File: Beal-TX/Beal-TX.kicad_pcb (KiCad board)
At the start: 2 copper layers, 37.1 x 56.9 mm, 64 parts, among them J1 CONMHF1-SMD-T, J3 Conn_02x04_Odd_Even, J4 Conn_02x04_Odd_Even, J5 UJ20-C-H-G-MSMT-4B-P16-TR, J6 Screw_Terminal_01x06, J7 TC2050, SW2 SW_Push, U150 LM5157-Q1, U2 TPSM863253, U5 LoRa-E5, U6 DRV8912QPWPRQ1

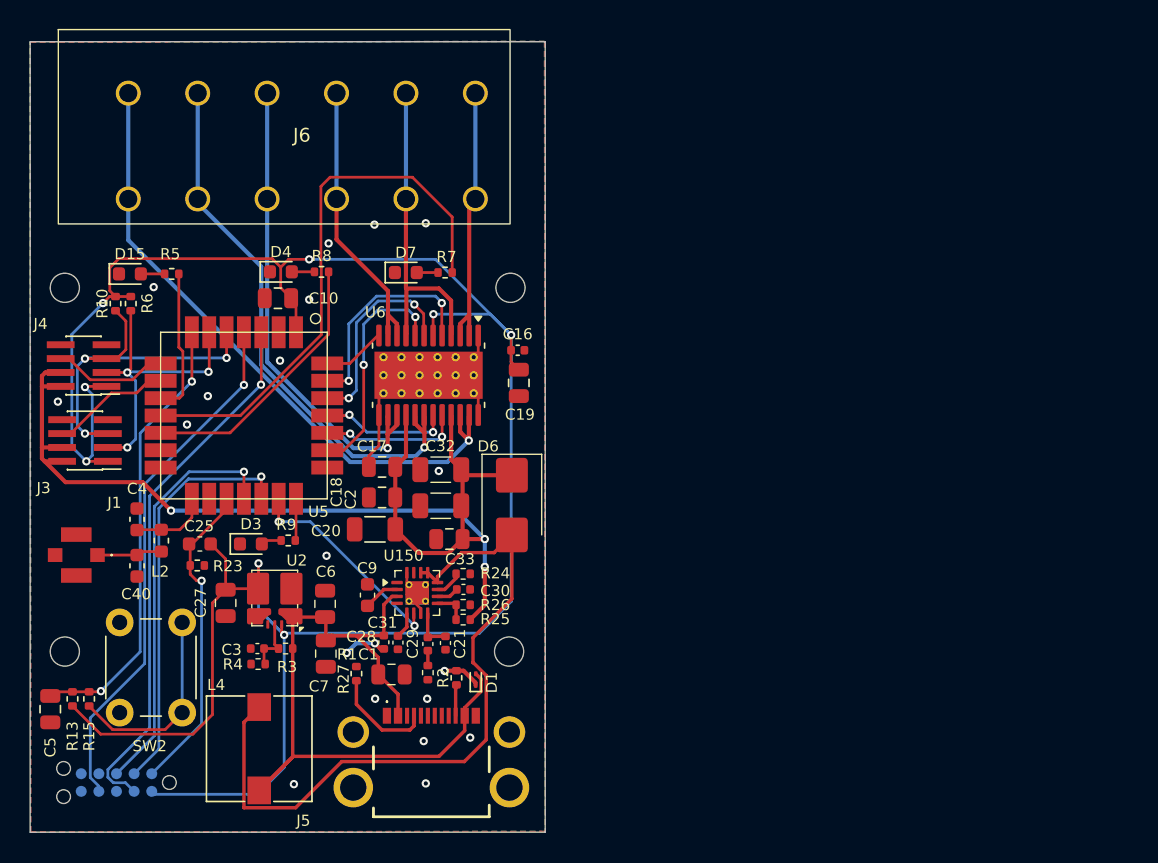
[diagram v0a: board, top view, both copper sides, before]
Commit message: Beal TX: Address some issues found during prototyping phase
Basically, the prototyping phase has highlighted some issues.
The major one is about the power delivered by an USB-C battery
is not enough to safely driver the valve.
The power after 9V decrease to about 5V, and the 5V from battery
fall to 2.0V.

One way for fixing it is using super capacitor.
This adds an extra cost to the BOM, and, I am not about its
duration regarding the operating conditions.

Because of the cost and the doubt about the longevity,
I would like to evaluate other solutions.
But, we also need to move forward so I made some changes to
power to make it more configurable so we could later try external
battery with a BMS, with different voltage with or without the booster.
By default we will have the super capacitor but we could slit main and
super capacitor board and plug a battery or any power source instead.

A minor change also introduced by this commit is adding testpoints.
Since the hardware an the software is not yet done, testpoints will
be very useful for debugging.

Signed-off-by: Alexandre Bailon <abailon@baylibre.com>
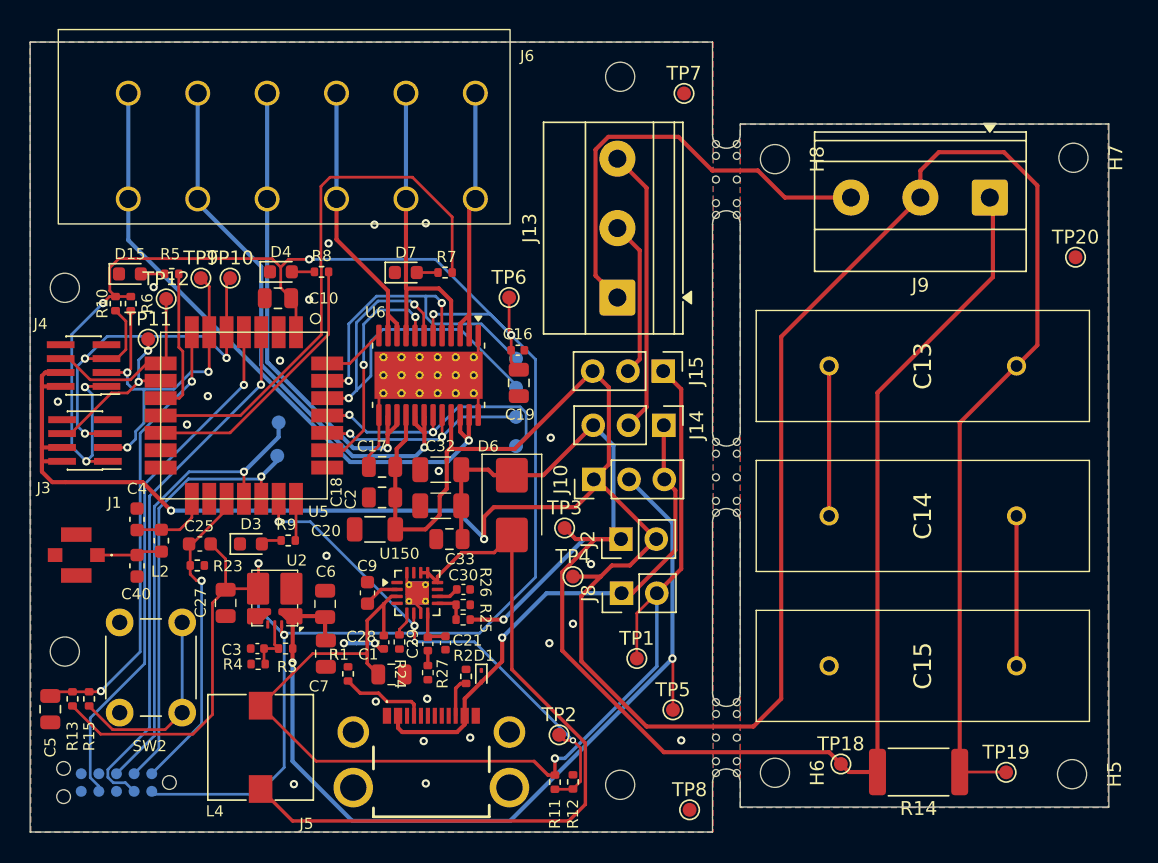
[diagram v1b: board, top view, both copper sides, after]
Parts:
- removed C31: 10nF, Capacitor_SMD:C_0402_1005Metric
- added B1: MouseBite, Panelization:MouseBite-Slot_2.0x4.5mm_outset_D0.5mm_P0.85mm_5h_Trace, F.Cu at (144.6, 19.9)
- added B2: MouseBite, Panelization:MouseBite-Slot_2.0x4.5mm_outset_D0.5mm_P0.85mm_5h_Trace, F.Cu at (144.7, 41.4)
- added B3: MouseBite, Panelization:MouseBite-Slot_2.0x4.5mm_outset_D0.5mm_P0.85mm_5h_Trace, F.Cu at (144.6, 60.1)
- added C13: 0.33F, SCMR14L334SRBB0:SCMR14L334SRBB0, F.Cu at (164.6, 33.3)
- added C14: 0.33F, SCMR14L334SRBB0:SCMR14L334SRBB0, F.Cu at (151.1, 44.1)
- added C15: 0.33F, SCMR14L334SRBB0:SCMR14L334SRBB0, F.Cu at (164.6, 54.9)
- added H5: MountingHole, MountingHole:MountingHole_2.1mm, F.Cu at (168.6, 62.7)
- added H6: MountingHole, MountingHole:MountingHole_2.1mm, F.Cu at (147.2, 62.6)
- added H7: MountingHole, MountingHole:MountingHole_2.1mm, F.Cu at (168.7, 18.3)
- added H8: MountingHole, MountingHole:MountingHole_2.1mm, F.Cu at (147.2, 18.4)
- added J10: Conn_01x03, Connector_PinHeader_2.54mm:PinHeader_1x03_P2.54mm_Vertical, F.Cu at (134.1, 41.5)
- added J13: Screw_Terminal_01x03, TerminalBlock_Phoenix:TerminalBlock_Phoenix_MKDS-1,5-3_1x03_P5.00mm_Horizontal, F.Cu at (135.8, 28.4)
- added J14: Conn_01x03, Connector_PinHeader_2.54mm:PinHeader_1x03_P2.54mm_Vertical, F.Cu at (139.1, 37.6)
- added J15: Conn_01x03, Connector_PinHeader_2.54mm:PinHeader_1x03_P2.54mm_Vertical, F.Cu at (139.1, 33.7)
- added J2: Conn_01x02, Connector_PinHeader_2.54mm:PinHeader_1x02_P2.54mm_Vertical, F.Cu at (136.1, 45.8)
- added J8: Conn_01x02, Connector_PinHeader_2.54mm:PinHeader_1x02_P2.54mm_Vertical, F.Cu at (136.1, 49.7)
- added J9: Screw_Terminal_01x03, TerminalBlock_Phoenix:TerminalBlock_Phoenix_MKDS-1,5-3_1x03_P5.00mm_Horizontal, F.Cu at (162.6, 21.2)
- added R11: 143k, Resistor_SMD:R_0402_1005Metric, F.Cu at (131.3, 63.3)
- added R12: 66.5k, Resistor_SMD:R_0402_1005Metric, F.Cu at (132.6, 63.3)
- added R14: 30, Resistor_SMD:R_2512_6332Metric, F.Cu at (157.5, 62.6)
- added TP1: TestPoint, TestPoint:TestPoint_Pad_D1.0mm, F.Cu at (137.2, 54.4)
- added TP10: TestPoint, TestPoint:TestPoint_Pad_D1.0mm, F.Cu at (107.9, 27.0)
- added TP11: TestPoint, TestPoint:TestPoint_Pad_D1.0mm, F.Cu at (102.0, 31.4)
- added TP12: TestPoint, TestPoint:TestPoint_Pad_D1.0mm, F.Cu at (103.3, 28.5)
- added TP13: TestPoint, TestPoint:TestPoint_Pad_D1.0mm, B.Cu at (128.5, 32.8)
- added TP14: TestPoint, TestPoint:TestPoint_Pad_D1.0mm, B.Cu at (128.5, 34.9)
- added TP15: TestPoint, TestPoint:TestPoint_Pad_D1.0mm, B.Cu at (128.5, 39.1)
- added TP16: TestPoint, TestPoint:TestPoint_Pad_D1.0mm, B.Cu at (128.5, 37.0)
- added TP18: TestPoint, TestPoint:TestPoint_Pad_D1.0mm, F.Cu at (151.9, 62.0)
- added TP19: TestPoint, TestPoint:TestPoint_Pad_D1.0mm, F.Cu at (163.8, 62.6)
- added TP2: TestPoint, TestPoint:TestPoint_Pad_D1.0mm, F.Cu at (131.6, 59.9)
- added TP20: TestPoint, TestPoint:TestPoint_Pad_D1.0mm, F.Cu at (168.8, 25.5)
- added TP21: TestPoint, TestPoint:TestPoint_Pad_D1.0mm, B.Cu at (111.3, 39.8)
- added TP22: TestPoint, TestPoint:TestPoint_Pad_D1.0mm, B.Cu at (111.4, 37.4)
- added TP3: TestPoint, TestPoint:TestPoint_Pad_D1.0mm, F.Cu at (132.0, 45.0)
- added TP4: TestPoint, TestPoint:TestPoint_Pad_D1.0mm, F.Cu at (132.6, 48.5)
- added TP5: TestPoint, TestPoint:TestPoint_Pad_D1.0mm, F.Cu at (139.8, 58.1)
- added TP6: TestPoint, TestPoint:TestPoint_Pad_D1.0mm, F.Cu at (128.0, 28.4)
- added TP7: TestPoint, TestPoint:TestPoint_Pad_D1.0mm, F.Cu at (140.6, 13.7)
- added TP8: TestPoint, TestPoint:TestPoint_Pad_D1.0mm, F.Cu at (141.0, 65.3)
- added TP9: TestPoint, TestPoint:TestPoint_Pad_D1.0mm, F.Cu at (105.8, 27.0)
- C30: value 10nF -> 4.7uF
- U150: footprint Beal:WQFN-16-1EP_3x3mm_P0.5mm_EP1.68x1.68mm_ThermalVias -> Package_DFN_QFN:WQFN-16-1EP_3x3mm_P0.5mm_EP1.68x1.68mm_ThermalVias
- moved H1 17.1 mm to (136.0, 12.5)
- moved H3 12.5 mm to (136.0, 63.5)
- moved R24 6.72 mm to (120.1, 53.2), turned to -90 degrees
- moved R2 0.70 mm to (124.9, 55.7)
- moved R1 0.60 mm to (116.4, 55.5)
- moved D1 0.47 mm to (126.0, 55.7), turned to -90 degrees
- moved C9 0.16 mm to (117.8, 49.7)
- moved L4 0.14 mm to (110.1, 60.8), turned to -90 degrees
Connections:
- C1 pad 1: VBUS -> Net-(J15-Pin_1)
- C2 pad 1: +9V -> +9V_Boost
- C28 pad 2: VBUS -> Net-(J15-Pin_1)
- C32 pad 1: +9V -> +9V_Boost
- C33 pad 1: +9V -> +9V_Boost
- C6 pad 1: VBUS -> Net-(J10-Pin_2)
- C7 pad 1: VBUS -> Net-(J10-Pin_2)
- D6 pad 1: +9V -> +9V_Boost
- L4 pad 1: VBUS -> Net-(J15-Pin_1)
- R24 pad 1: Net-(R24-Pad1) -> Net-(U150-RT)
- R25 pad 1: +9V -> +9V_Boost
- R3 pad 1: VBUS -> Net-(J10-Pin_2)
- U150 pad 11: Net-(R24-Pad1) -> GND
- U150 pad 3: VBUS -> Net-(J15-Pin_1)
- U150 pad 5: Net-(C31-Pad1) -> Net-(U150-RT)
- U2 pad 1: VBUS -> Net-(J10-Pin_2)
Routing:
- net +9V: track 81.0 -> 235.8 mm, vias 3 -> 2
- net +9V_Boost: track 0.00 -> 125.2 mm, vias 0 -> 1
- net Net-(J15-Pin_1): track 0.00 -> 81.0 mm, vias 0 -> 1
- net Net-(J10-Pin_2): track 0.00 -> 66.5 mm, vias 0 -> 2
- net GND: track 18.4 -> 47.4 mm, vias 20 -> 24
- net 9V_EN: track 15.5 -> 37.4 mm, vias 2 -> 4
- net Net-(J13-Pin_3): track 0.00 -> 20.6 mm
- net VBUS: track 56.1 -> 37.8 mm, vias 0 -> 1
- net MISO_EXT_3_OUT: track 14.6 -> 31.2 mm
- net Net-(J13-Pin_2): track 0.00 -> 11.3 mm
- net Net-(C14-Pad2): track 0.00 -> 10.8 mm
- net Net-(C13-Pad2): track 0.00 -> 10.8 mm
- net CS_EXT_3_OUT: track 9.31 -> 19.6 mm
- net MOSI_EXT_3_OUT: track 15.7 -> 24.9 mm
- net SCLK_EXT_3_OUT: track 10.0 -> 16.0 mm
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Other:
- board size 37.1 x 56.9 mm -> 77.7 x 56.9 mm

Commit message: Beal-TX: Remove changes previoulsy done regarding done regarding battery tests
I made some measurement on comptitor product and finaly,
the signal to control the valve is not that bad.
I have decided to just add a capacitor and to remove all the
tests features added by previous commit.

This also tries to address some potential issues and does some
improvements such as increasing traces for VBUS and +9V.

Signed-off-by: Alexandre Bailon <abailon@baylibre.com>
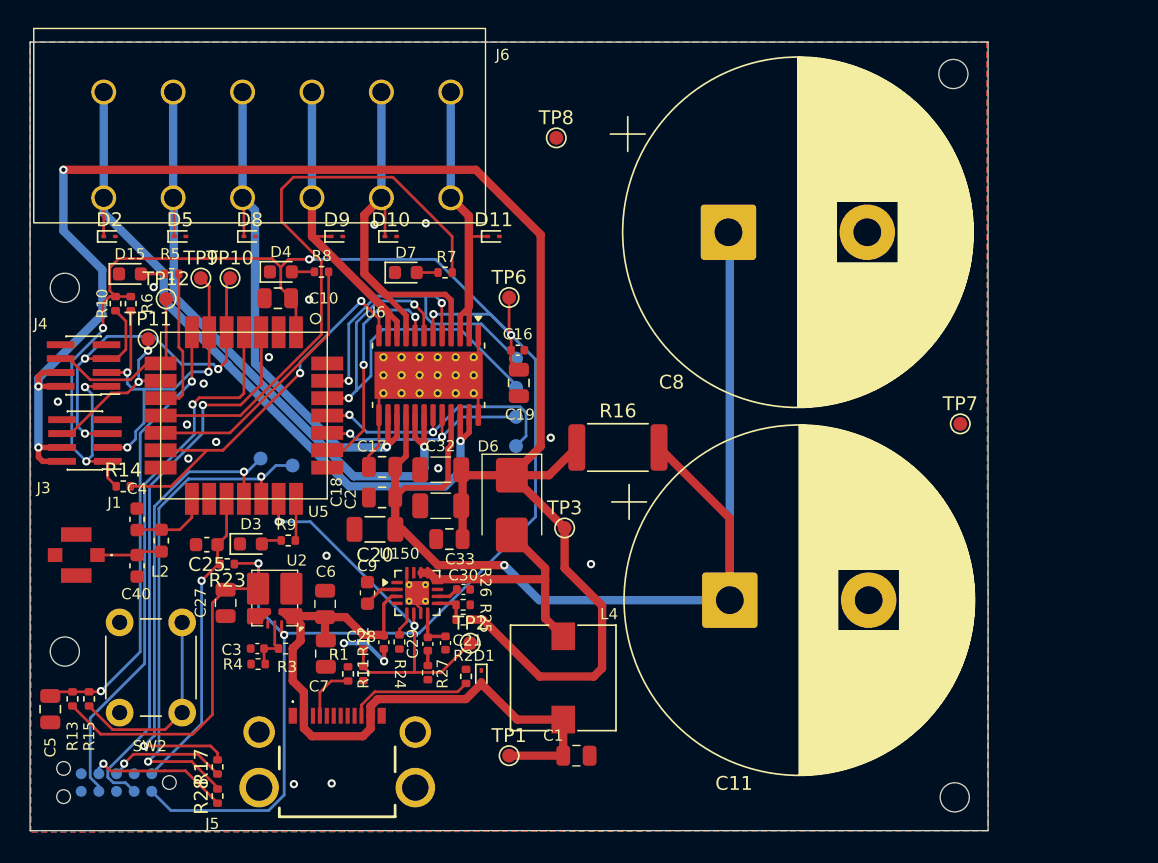
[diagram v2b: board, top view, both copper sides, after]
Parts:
- removed B1, B2, B3: MouseBite, Panelization:MouseBite-Slot_2.0x4.5mm_outset_D0.5mm_P0.85mm_5h_Trace
- removed C13, C14, C15: 0.33F, SCMR14L334SRBB0:SCMR14L334SRBB0
- removed H5, H6, H7, H8: MountingHole, MountingHole:MountingHole_2.1mm
- removed J10, J14, J15: Conn_01x03, Connector_PinHeader_2.54mm:PinHeader_1x03_P2.54mm_Vertical
- removed J13, J9: Screw_Terminal_01x03, TerminalBlock_Phoenix:TerminalBlock_Phoenix_MKDS-1,5-3_1x03_P5.00mm_Horizontal
- removed J2, J8: Conn_01x02, Connector_PinHeader_2.54mm:PinHeader_1x02_P2.54mm_Vertical
- removed TP18, TP19, TP20, TP4, TP5: TestPoint, TestPoint:TestPoint_Pad_D1.0mm
- added C11: 8.2mF, Capacitor_THT:CP_Radial_D25.0mm_P10.00mm_SnapIn, F.Cu at (143.9, 50.2)
- added C8: 8.2mF, Capacitor_THT:CP_Radial_D25.0mm_P10.00mm_SnapIn, F.Cu at (143.8, 23.7)
- added D10: ESD9X12ST5G, Diode_SMD:D_SOD-923, F.Cu at (119.5, 24.0)
- added D11: ESD9X12ST5G, Diode_SMD:D_SOD-923, F.Cu at (126.9, 24.0)
- added D2: ESD9X12ST5G, Diode_SMD:D_SOD-923, F.Cu at (99.2, 24.0)
- added D5: ESD9X12ST5G, Diode_SMD:D_SOD-923, F.Cu at (104.3, 24.0)
- added D8: ESD9X12ST5G, Diode_SMD:D_SOD-923, F.Cu at (109.3, 24.0)
- added D9: ESD9X12ST5G, Diode_SMD:D_SOD-923, F.Cu at (115.6, 24.0)
- added R16: 30, Resistor_SMD:R_2512_6332Metric, F.Cu at (135.8, 39.2)
- added R17: 0, Resistor_SMD:R_0402_1005Metric, F.Cu at (107.0, 62.2)
- added R28: 0, Resistor_SMD:R_0402_1005Metric, F.Cu at (107.0, 64.3)
- C20: footprint Resistor_SMD:R_1206_3216Metric -> Capacitor_SMD:C_1206_3216Metric
- C27: value 23uF -> 22uF
- R14: value 30 -> 10K; footprint Resistor_SMD:R_2512_6332Metric -> Resistor_SMD:R_0402_1005Metric
- moved R14 60.9 mm to (100.2, 42.0), turned to 0 degrees
- moved TP8 49.3 mm to (131.4, 16.9)
- moved TP7 31.0 mm to (160.5, 37.5)
- moved H3 24.1 mm to (160.1, 64.4)
- moved H1 24.0 mm to (160.0, 12.3)
- moved L4 22.4 mm to (131.9, 55.8), turned to 90 degrees
- moved R11 17.1 mm to (117.5, 53.2)
- moved R12 17.0 mm to (117.5, 55.5), turned to -90 degrees
- moved C1 14.6 mm to (132.9, 61.4)
- moved TP1 11.6 mm to (128.0, 61.4)
- moved TP2 9.19 mm to (125.2, 53.3)
- moved J5 6.78 mm to (115.6, 62.2)
- moved TP22 2.91 mm to (110.1, 40.0)
- moved R23 2.16 mm to (107.7, 47.6), turned to 180 degrees
- moved J6 1.77 mm to (111.3, 17.4)
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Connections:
- C1 pad 1: Net-(J15-Pin_1) -> VBUS
- C17 pad 1: +9V -> +9V_VM
- C18 pad 1: +9V -> +9V_VM
- C2 pad 1: +9V_Boost -> +9V
- C20 pad 1: +9V -> +9V_VM
- C25 pad 1: +3.3V -> WIO_RESET
- C25 pad 2: WIO_RESET -> GND
- C28 pad 2: Net-(J15-Pin_1) -> VBUS
- C32 pad 1: +9V_Boost -> +9V
- C33 pad 1: +9V_Boost -> +9V
- C6 pad 1: Net-(J10-Pin_2) -> VBUS
- C7 pad 1: Net-(J10-Pin_2) -> VBUS
- D6 pad 1: +9V_Boost -> +9V
- J5 pad MH1: unconnected-(J5-MH_1-PadMH1) -> GND
- J5 pad MH2: unconnected-(J5-MH_2-PadMH2) -> GND
- J5 pad MH3: unconnected-(J5-MH_3-PadMH3) -> GND
- J5 pad MH4: unconnected-(J5-MH_4-PadMH4) -> GND
- J7 pad 7: unconnected-(J7-Pad7) -> Net-(J7-Pad7)
- J7 pad 8: E5_RX -> Net-(J7-Pad8)
- J7 pad 9: E5_TX -> unconnected-(J7-Pad9)
- L4 pad 1: Net-(J15-Pin_1) -> VBUS
- R11 pad 1: Net-(J15-Pin_1) -> VBUS
- R14 pad 1: +9V -> +3.3V
- R14 pad 2: +9V_Boost -> MCU_FAULT_N
- R23 pad 1: WIO_RESET -> +3.3V
- R23 pad 2: GND -> WIO_RESET
- R25 pad 1: +9V_Boost -> +9V
- R3 pad 1: Net-(J10-Pin_2) -> VBUS
- TP1 pad 1: Net-(J15-Pin_1) -> VBUS
- TP3 pad 1: +9V_Boost -> +9V
- U150 pad 3: Net-(J15-Pin_1) -> VBUS
- U2 pad 1: Net-(J10-Pin_2) -> VBUS
- U5 pad 13: unconnected-(U5-PC0-Pad13) -> MCU_FAULT_N
- U5 pad 28: MCU_FAULT_N -> unconnected-(U5-PB0-Pad28)
- U6 pad 16: +9V -> +9V_VM
- U6 pad 21: +9V -> +9V_VM
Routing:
- net +9V_Boost: track 125.2 -> 0.00 mm, vias 1 -> 0
- net +9V: track 235.8 -> 128.2 mm, vias 2 -> 3
- net +9V_VM: track 0.00 -> 83.6 mm, vias 0 -> 1
- net Net-(J15-Pin_1): track 81.0 -> 0.00 mm, vias 1 -> 0
- net Net-(J10-Pin_2): track 66.5 -> 0.00 mm, vias 2 -> 0
- net Net-(D6-A): track 55.0 -> 20.5 mm
- net GND: track 47.4 -> 16.8 mm, vias 24 -> 18
- net MCU_FAULT_N: track 4.59 -> 29.0 mm, vias 0 -> 2
- net Net-(J13-Pin_3): track 20.6 -> 0.00 mm
- net VBUS: track 37.8 -> 50.4 mm, vias 1 -> 0
- net Net-(J13-Pin_2): track 11.3 -> 0.00 mm
- net Net-(C14-Pad2): track 10.8 -> 0.00 mm
- net Net-(C13-Pad2): track 10.8 -> 0.00 mm
- net Net-(J7-Pad7): track 0.00 -> 10.3 mm, vias 0 -> 1
- net 9V_EN: track 37.4 -> 28.8 mm, vias 4 -> 2
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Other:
- board size 77.7 x 56.9 mm -> 69 x 56.8 mm
